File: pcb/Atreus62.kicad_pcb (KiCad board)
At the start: 2 copper layers, 270.1 x 112.9 mm, 125 parts, among them SW1 SWITCH_PUSH, SW10 SWITCH_PUSH, SW11 SWITCH_PUSH, SW12 SWITCH_PUSH, SW13 SWITCH_PUSH, SW14 SWITCH_PUSH, SW15 SWITCH_PUSH, SW16 SWITCH_PUSH, SW17 SWITCH_PUSH, SW18 SWITCH_PUSH, SW19 SWITCH_PUSH, SW2 SWITCH_PUSH, SW20 SWITCH_PUSH, SW21 SWITCH_PUSH, SW22 SWITCH_PUSH, SW23 SWITCH_PUSH, SW24 SWITCH_PUSH, SW25 SWITCH_PUSH, SW26 SWITCH_PUSH, SW27 SWITCH_PUSH, SW28 SWITCH_PUSH, SW29 SWITCH_PUSH, SW3 SWITCH_PUSH, SW30 SWITCH_PUSH, SW31 SWITCH_PUSH, SW32 SWITCH_PUSH, SW33 SWITCH_PUSH, SW34 SWITCH_PUSH, SW35 SWITCH_PUSH, SW36 SWITCH_PUSH, SW37 SWITCH_PUSH, SW38 SWITCH_PUSH, SW39 SWITCH_PUSH, SW4 SWITCH_PUSH, SW40 SWITCH_PUSH, SW41 SWITCH_PUSH, SW42 SWITCH_PUSH, SW43 SWITCH_PUSH, SW44 SWITCH_PUSH, SW45 SWITCH_PUSH, SW46 SWITCH_PUSH, SW47 SWITCH_PUSH, SW48 SWITCH_PUSH, SW49 SWITCH_PUSH, SW5 SWITCH_PUSH, SW50 SWITCH_PUSH, SW51 SWITCH_PUSH, SW52 SWITCH_PUSH, SW53 SWITCH_PUSH, SW54 SWITCH_PUSH, SW55 SWITCH_PUSH, SW56 SWITCH_PUSH, SW57 SWITCH_PUSH, SW58 SWITCH_PUSH, SW59 SWITCH_PUSH, SW6 SWITCH_PUSH, SW60 SWITCH_PUSH, SW61 SWITCH_PUSH, SW62 SWITCH_PUSH, SW7 SWITCH_PUSH, SW8 SWITCH_PUSH, SW9 SWITCH_PUSH, U1 ARDUINO_PRO_MICRO

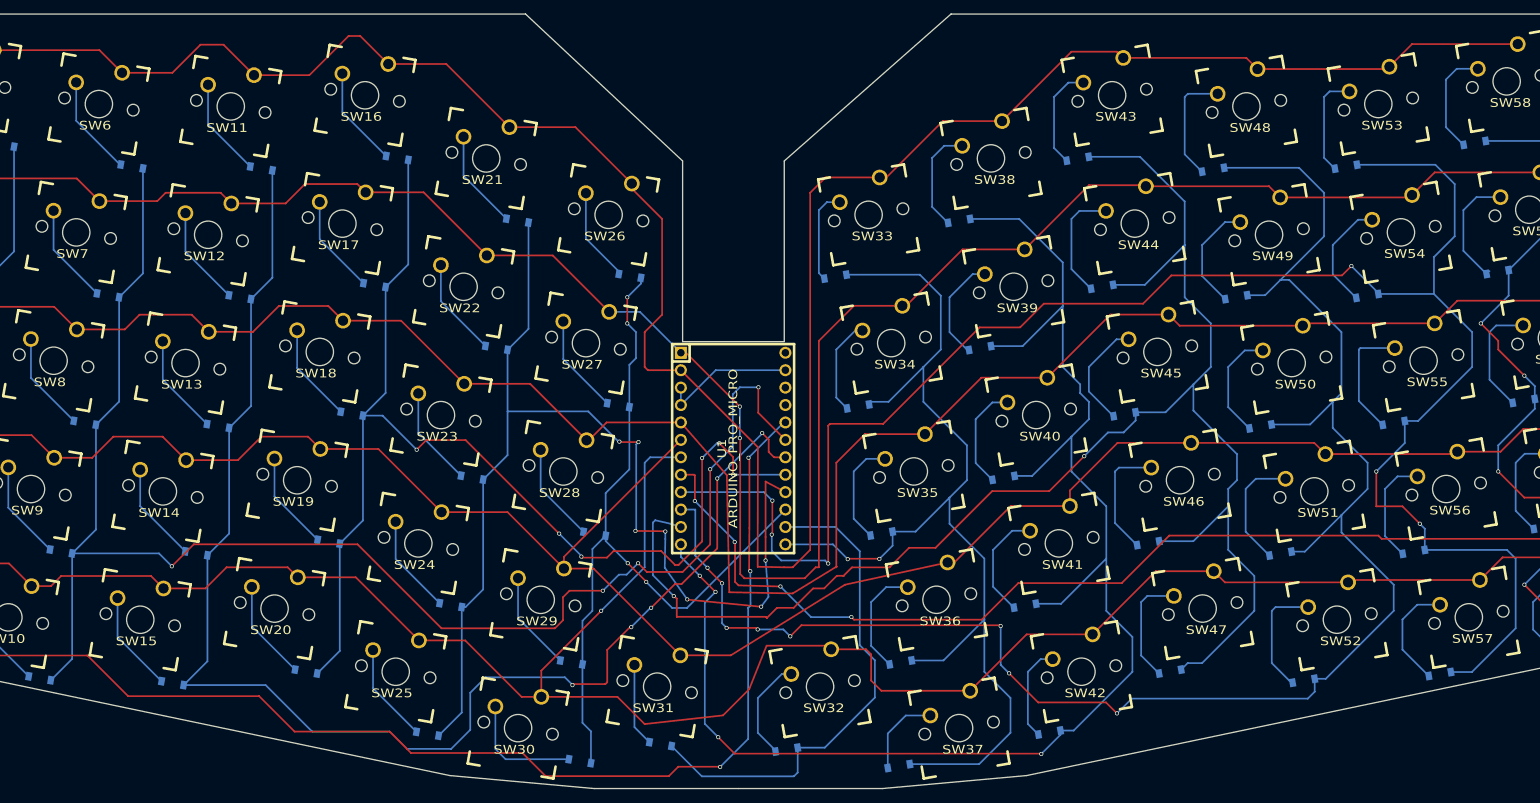
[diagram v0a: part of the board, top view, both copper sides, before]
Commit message: Adding reset switch to PCB
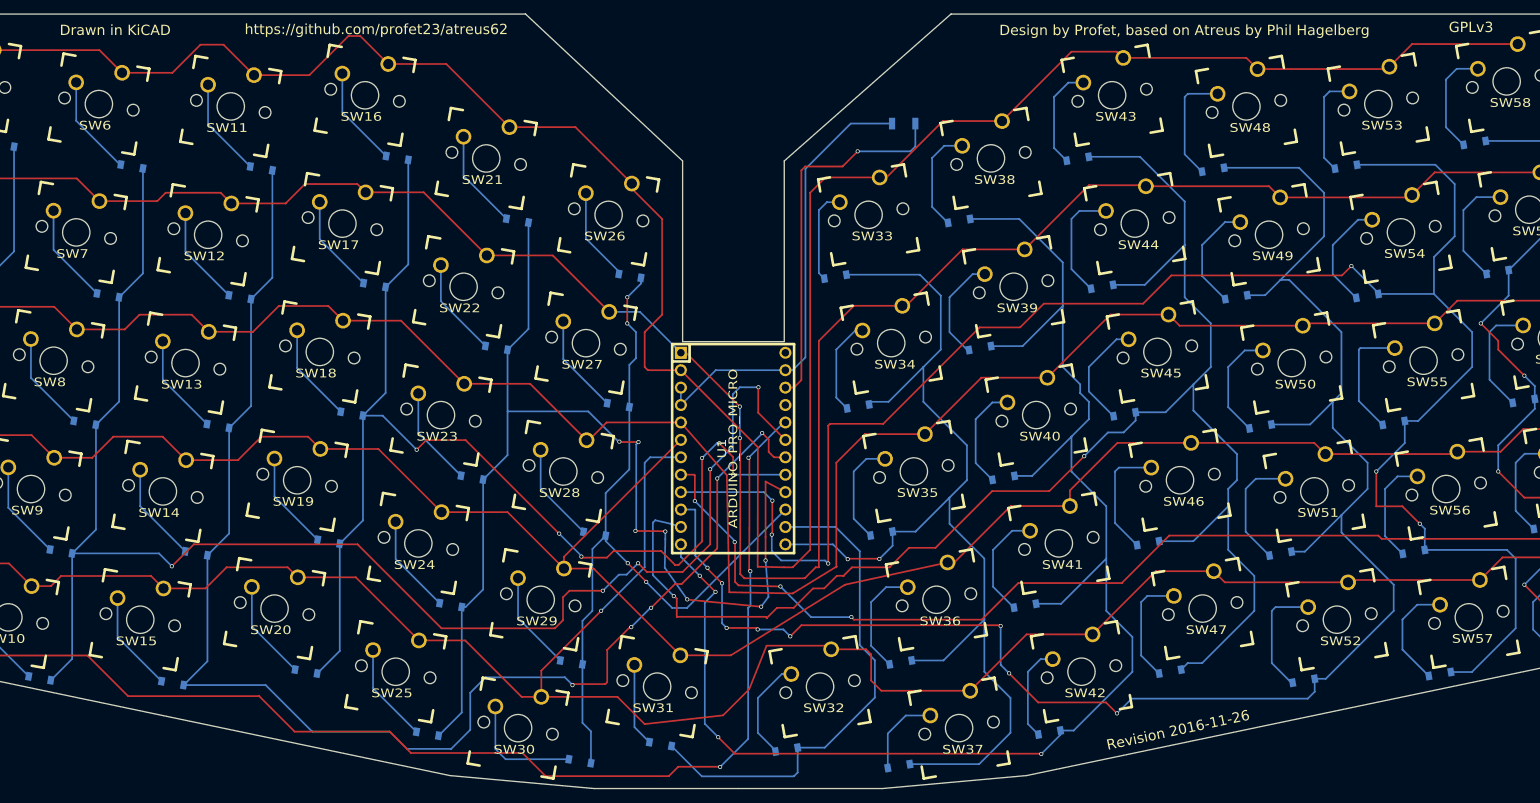
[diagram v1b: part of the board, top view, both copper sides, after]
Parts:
- added SW-RST1: SWITCH_PUSH, Buttons_Switches_SMD:SW_SPST_B3U-1000P, B.Cu at (172.4, 57.2)
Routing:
- net Net-(SW-RST1-Pad2): track 0.00 -> 54.8 mm, vias 0 -> 1
- net GND: track 19.9 -> 66.4 mm
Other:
- board text added: "Design by Profet, based on Atreus by Phil Hagelberg"
- board text added: "Drawn in KiCAD"
- board text added: "GPLv3"
- board text added: "Revision 2016-11-26"
- board text added: "https://github.com/profet23/atreus62"
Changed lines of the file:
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@@
 (kicad_pcb (version 4) (host pcbnew 4.0.4-stable)
   (general
-    (links 188)
+    (links 190)
     (no_connects 0)
-    (area 11.966657 39.907645 284.668017 156.536874)
+    (area 13.145017 41.201456 283.393012 154.230442)
     (thickness 1.6)
-    (drawings 1256)
-    (tracks 909)
+    (drawings 1261)
+    (tracks 924)
     (zones 0)
-    (modules 125)
+    (modules 126)
     (nets 85)
   )
@@
   (net 81 GND)
   (net 82 VCC)
-  (net 83 "Net-(U1-Pad22)")
-  (net 84 "Net-(U1-Pad24)")
+  (net 83 "Net-(U1-Pad24)")
+  (net 84 "Net-(SW-RST1-Pad2)")
   (net_class Default "This is the default net class."
     (clearance 0.2)
@@
     (add_net "Net-(D8-Pad1)")
     (add_net "Net-(D9-Pad1)")
-    (add_net "Net-(U1-Pad22)")
+    (add_net "Net-(SW-RST1-Pad2)")
     (add_net "Net-(U1-Pad24)")
     (add_net VCC)
@@
       (net 82 VCC))
     (pad 22 thru_hole circle (at -8.89 -7.62 270) (size 1.7526 1.7526) (drill 1.0922) (layers *.Cu *.SilkS *.Mask)
-      (net 83 "Net-(U1-Pad22)"))
+      (net 84 "Net-(SW-RST1-Pad2)"))
     (pad 23 thru_hole circle (at -11.43 -7.62 270) (size 1.7526 1.7526) (drill 1.0922) (layers *.Cu *.SilkS *.Mask)
       (net 81 GND))
@@
       (net 47 /COL8))
     (pad 24 thru_hole circle (at -13.97 -7.62 270) (size 1.7526 1.7526) (drill 1.0922) (layers *.Cu *.SilkS *.Mask)
-      (net 84 "Net-(U1-Pad24)"))
+      (net 83 "Net-(U1-Pad24)"))
+  )
+  (module Buttons_Switches_SMD:SW_SPST_B3U-1000P (layer B.Cu)
+    (at 172.39 57.22)
+    (descr "Ultra-small-sized Tactile Switch with High Contact Reliability, Top-actuated Model, without Ground Terminal, without Boss")
+    (tags "Tactile Switch")
+    (attr smd)
+    (fp_text reference SW-RST1 (at 0 2.5) (layer B.SilkS)
+      (effects (font (size 1 1) (thickness 0.15)) (justify mirror))
+    )
+    (fp_text value SWITCH_PUSH (at 0 -2.5) (layer B.Fab)
+      (effects (font (size 1 1) (thickness 0.15)) (justify mirror))
+    )
+    (fp_line (start -2.4 -1.65) (end 2.4 -1.65) (layer B.CrtYd) (width 0.05))
+    (fp_line (start 2.4 -1.65) (end 2.4 1.65) (layer B.CrtYd) (width 0.05))
+    (fp_line (start 2.4 1.65) (end -2.4 1.65) (layer B.CrtYd) (width 0.05))
+    (fp_line (start -2.4 1.65) (end -2.4 -1.65) (layer B.CrtYd) (width 0.05))
+    (fp_circle (center 0 0) (end 0.75 0) (layer B.SilkS) (width 0.15))
+    (fp_line (start -1.65 -1.1) (end -1.65 -1.4) (layer B.SilkS) (width 0.15))
+    (fp_line (start -1.65 -1.4) (end 1.65 -1.4) (layer B.SilkS) (width 0.15))
+    (fp_line (start 1.65 -1.4) (end 1.65 -1.1) (layer B.SilkS) (width 0.15))
+    (fp_line (start -1.65 1.1) (end -1.65 1.4) (layer B.SilkS) (width 0.15))
+    (fp_line (start -1.65 1.4) (end 1.65 1.4) (layer B.SilkS) (width 0.15))
+    (fp_line (start 1.65 1.4) (end 1.65 1.1) (layer B.SilkS) (width 0.15))
+    (fp_line (start -1.5 1.25) (end 1.5 1.25) (layer B.Fab) (width 0.15))
+    (fp_line (start 1.5 1.25) (end 1.5 -1.25) (layer B.Fab) (width 0.15))
+    (fp_line (start 1.5 -1.25) (end -1.5 -1.25) (layer B.Fab) (width 0.15))
+    (fp_line (start -1.5 -1.25) (end -1.5 1.25) (layer B.Fab) (width 0.15))
+    (pad 1 smd rect (at -1.7 0) (size 0.9 1.7) (layers B.Cu B.Paste B.Mask)
+      (net 81 GND))
+    (pad 2 smd rect (at 1.7 0) (size 0.9 1.7) (layers B.Cu B.Paste B.Mask)
+      (net 84 "Net-(SW-RST1-Pad2)"))
+  )
+  (gr_text "Revision 2016-11-26" (at 212.4 145.65 12) (layer F.SilkS)
+    (effects (font (size 1.5 1.5) (thickness 0.3)))
+  )
+  (gr_text https://github.com/profet23/atreus62 (at 95.49 43.48) (layer F.SilkS)
+    (effects (font (size 1.5 1.5) (thickness 0.3)))
+  )
+  (gr_text GPLv3 (at 255.12 43.18) (layer F.SilkS)
+    (effects (font (size 1.5 1.5) (thickness 0.3)))
+  )
+  (gr_text "Drawn in KiCAD" (at 57.42 43.61) (layer F.SilkS)
+    (effects (font (size 1.5 1.5) (thickness 0.3)))
+  )
+  (gr_text "Design by Profet, based on Atreus by Phil Hagelberg" (at 213.33 43.62) (layer F.SilkS)
+    (effects (font (size 1.5 1.5) (thickness 0.3)))
   )
   (gr_text atreus62 (at 148.34 126.44) (layer B.SilkS)
@@
   (segment (start 167.64 134.62) (end 166.89611 133.87611) (width 0.25) (layer F.Cu) (net 80))
   (segment (start 166.89611 133.87611) (end 161.813953 133.87611) (width 0.25) (layer F.Cu) (net 80))
+  (segment (start 170.69 57.22) (end 164.67 57.22) (width 0.25) (layer B.Cu) (net 81) (status 400000))
+  (segment (start 156.19 93.18) (end 155.14 93.18) (width 0.25) (layer B.Cu) (net 81) (status 800000))
+  (segment (start 158.06 91.31) (end 156.19 93.18) (width 0.25) (layer B.Cu) (net 81))
+  (segment (start 158.06 63.83) (end 158.06 91.31) (width 0.25) (layer B.Cu) (net 81))
+  (segment (start 164.67 57.22) (end 158.06 63.83) (width 0.25) (layer B.Cu) (net 81))
   (segment (start 139.9 95.72) (end 139.9 98.26) (width 0.25) (layer B.Cu) (net 81))
   (segment (start 139.9 98.26) (end 144.98 93.18) (width 0.25) (layer B.Cu) (net 81))
   (segment (start 144.98 93.18) (end 155.14 93.18) (width 0.25) (layer B.Cu) (net 81))
+  (segment (start 174.09 57.22) (end 174.09 60.55) (width 0.25) (layer B.Cu) (net 84) (status 400000))
+  (segment (start 156.38 95.72) (end 155.14 95.72) (width 0.25) (layer F.Cu) (net 84) (status 800000))
+  (segment (start 157.47 94.63) (end 156.38 95.72) (width 0.25) (layer F.Cu) (net 84))
+  (segment (start 157.47 64.04) (end 157.47 94.63) (width 0.25) (layer F.Cu) (net 84))
+  (segment (start 158.03 63.48) (end 157.47 64.04) (width 0.25) (layer F.Cu) (net 84))
+  (segment (start 163.47 63.48) (end 158.03 63.48) (width 0.25) (layer F.Cu) (net 84))
+  (segment (start 165.68 61.27) (end 163.47 63.48) (width 0.25) (layer F.Cu) (net 84))
+  (via (at 165.68 61.27) (size 0.6) (drill 0.4) (layers F.Cu B.Cu) (net 84))
+  (segment (start 173.37 61.27) (end 165.68 61.27) (width 0.25) (layer B.Cu) (net 84))
+  (segment (start 174.09 60.55) (end 173.37 61.27) (width 0.25) (layer B.Cu) (net 84))
 )

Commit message: Merging in changes from NaCly
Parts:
- added G***: LOGO, footprints:profetkeyboards_logo, B.Cu at (148.2, 127.0)
- added J6 (x2): D2, keebio:SinglePad, F.Cu at (177.6, 45.8)
- D1, D10, D11, D12, D13, D14, D15, D16, D17, D18, D19, D20, D21, D22, D23, D24, D25, D26, D27, D28, D29, D3, D30, D31, D32, D33, D34, D35, D36, D37, D38, D39, D4, D40, D41, D42, D43, D44, D45, D46, D47, D48, D49, D5, D50, D51, D52, D53, D54, D55, D56, D57, D58, D59, D6, D60, D61, D62, D7, D8, D9: footprint Diodes_SMD:SOD-123 -> keebio:Diode-Hybrid-Back; moved to F.Cu
- D2: footprint Diodes_SMD:SOD-123 -> keebio:Diode-Hybrid-Back
- SW1, SW10, SW11, SW12, SW13, SW14, SW15, SW16, SW17, SW18, SW19, SW2, SW20, SW21, SW22, SW23, SW24, SW25, SW26, SW27, SW28, SW29, SW3, SW30, SW31, SW32, SW33, SW34, SW35, SW36, SW37, SW38, SW39, SW4, SW40, SW41, SW42, SW43, SW44, SW45, SW46, SW47, SW48, SW49, SW5, SW50, SW51, SW52, SW53, SW54, SW55, SW56, SW57, SW58, SW59, SW6, SW60, SW61, SW62, SW7, SW8, SW9: footprint footprints:CHERRY_PCB_100H -> keebio:MX-Alps-Choc-1U-NoLED
- moved D31 11.9 mm to (145.8, 139.9), turned to 270 degrees
- moved D32 9.81 mm to (150.7, 139.9), turned to 270 degrees
- moved D37 7.74 mm to (164.1, 152.4), turned to 0 degrees
- moved D30 7.01 mm to (131.8, 152.4), turned to 0 degrees
- moved D36 6.98 mm to (178.8, 134.3)
- moved D43 6.80 mm to (204.4, 60.8)
- moved D54 6.71 mm to (246.5, 80.8)
- moved D41 6.69 mm to (196.6, 126.1)
- moved D51 6.69 mm to (233.9, 118.5)
- moved D48 6.65 mm to (224.0, 62.4)
- moved D22 6.63 mm to (106.7, 88.1)
- moved D39 6.61 mm to (190.0, 88.7)
- moved D33 6.59 mm to (168.9, 78.2)
- moved D52 6.58 mm to (237.2, 137.2)
- moved D24 6.57 mm to (100.1, 125.5)
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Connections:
- SW31 pad 1: /ROW1 -> /ROW0
- SW32 pad 1: /ROW0 -> /ROW1
- U1 pad 1: /ROW3 -> /ROW4
- U1 pad 10: /COL10 -> /COL2
- U1 pad 11: /COL9 -> /COL3
- U1 pad 12: /COL8 -> /COL4
- U1 pad 13: /COL7 -> /COL5
- U1 pad 15: /COL5 -> /COL7
- U1 pad 16: /COL4 -> /COL8
- U1 pad 17: /COL3 -> /COL9
- U1 pad 18: /COL2 -> /COL10
- U1 pad 19: /COL1 -> /COL11
- U1 pad 2: /ROW4 -> /ROW3
- U1 pad 20: /COL0 -> /COL12
- U1 pad 8: /COL12 -> /COL0
- U1 pad 9: /COL11 -> /COL1
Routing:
- net /ROW3: track 316.2 -> 458.6 mm
- net /ROW4: track 353.1 -> 495.3 mm, vias 0 -> 2
- net /ROW2: track 297.3 -> 439.3 mm, vias 0 -> 2
- net /ROW1: track 300.5 -> 432.7 mm, vias 0 -> 2
- net /ROW0: track 328.4 -> 456.8 mm, vias 1 -> 0
- net /COL8: track 217.0 -> 138.4 mm, vias 4 -> 2
- net /COL11: track 270.6 -> 201.8 mm, vias 6 -> 0
- net /COL9: track 232.8 -> 180.2 mm
- net /COL5: track 112.9 -> 146.7 mm, vias 4 -> 0
- net /COL10: track 252.7 -> 221.0 mm, vias 8 -> 5
- net /COL2: track 206.5 -> 175.4 mm, vias 5 -> 1
- net /COL0: track 258.1 -> 234.7 mm, vias 4 -> 2
- net /COL7: track 156.8 -> 133.6 mm, vias 2 -> 0
- net /COL6: track 72.9 -> 53.0 mm, vias 0 -> 2
- net Net-(D37-Pad1): track 12.3 -> 31.1 mm
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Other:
- board size 270.1 x 112.9 mm -> 270 x 113 mm
- board text added: "Design by Profet, based on Atreus by Phil Hagelberg. Contributions from NaCly"
- board text added: "Revision 2019-11-10"
- board text removed: "Design by Profet, based on Atreus by Phil Hagelberg"
- board text removed: "Revision 2016-11-26"
